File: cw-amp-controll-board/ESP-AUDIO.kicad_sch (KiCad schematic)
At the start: 0 parts

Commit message: finisched ESP32 Audio, started placement
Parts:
- added C10, C11, C16, C9: 100nF, Capacitor_SMD:C_0805_2012Metric_Pad1.18x1.45mm_HandSolder, symbol Device:C
- added C12, C13, C14, C15, C17, C18: 1µF, Capacitor_SMD:C_0805_2012Metric_Pad1.18x1.45mm_HandSolder, symbol Device:C
- added C8: 10µF, Capacitor_SMD:C_0805_2012Metric_Pad1.18x1.45mm_HandSolder, symbol Device:C
- added J4: Conn_01x03_Male, Connector_PinHeader_2.54mm:PinHeader_1x03_P2.54mm_Vertical, symbol Connector:Conn_01x03_Male
- added R19: 470R, Resistor_SMD:R_0805_2012Metric_Pad1.20x1.40mm_HandSolder, symbol Device:R
- added R20: ~, Resistor_SMD:R_0805_2012Metric_Pad1.20x1.40mm_HandSolder, symbol Device:R
- added STAR2: SolderJumper_2_Bridged, Jumper:SolderJumper-2_P1.3mm_Bridged_RoundedPad1.0x1.5mm, symbol Jumper:SolderJumper_2_Bridged
- added U6: PCM5100A, Package_SO:TSSOP-20_4.4x6.5mm_P0.65mm, symbol Audio:PCM5100
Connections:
- new net: C13.1, C15.1, U6.2 (CAPP)
- new net: C13.2, C15.2, U6.4 (CAPM)
- new net +3V3: C10.1, C11.1, C8.1, C9.1, U6.1 (CPVDD), U6.17 (XSMT), U6.20 (DVDD), U6.8 (AVDD)
- new net BCK: U6.13 (BCK)
- new net DIN: U6.14 (DIN)
- new net GNDA: C11.2, C17.2, C18.2, J4.2 (Pin_2), STAR2.2 (B), U6.9 (AGND)
- new net GNDD: C10.2, C12.2, C14.2, C16.2, C8.2, C9.2, STAR2.1 (A), U6.10 (DEMP), U6.11 (FLT), U6.16 (FMT), U6.19 (DGND), U6.3 (CPGND)
- new net L-OUT-ESP: C17.1, J4.1 (Pin_1), R19.2
- new net LDOO: C16.1, U6.18 (LDOO)
- new net LRCLK: U6.15 (LRCK)
- new net OUTL-PCM: R19.1, U6.6 (OUTL)
- new net OUTR-PCM: R20.1, U6.7 (OUTR)
- new net R-OUT-ESP: C18.1, J4.3 (Pin_3), R20.2
- new net SCK: U6.12 (SCK)
- new net VNEG: C12.1, C14.1, U6.5 (VNEG)

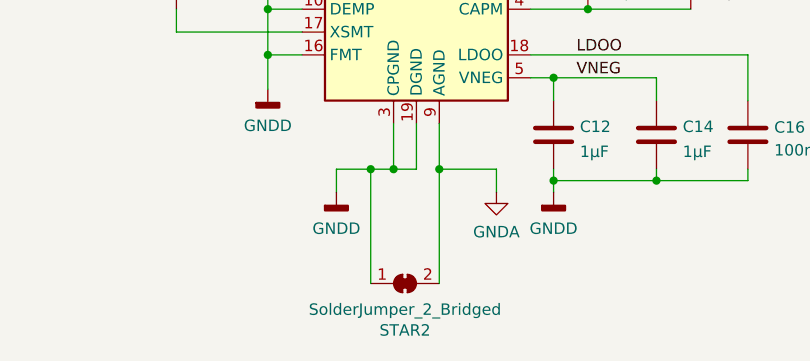
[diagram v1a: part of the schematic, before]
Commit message: reqork for 1.2, fix error with i2c port expander
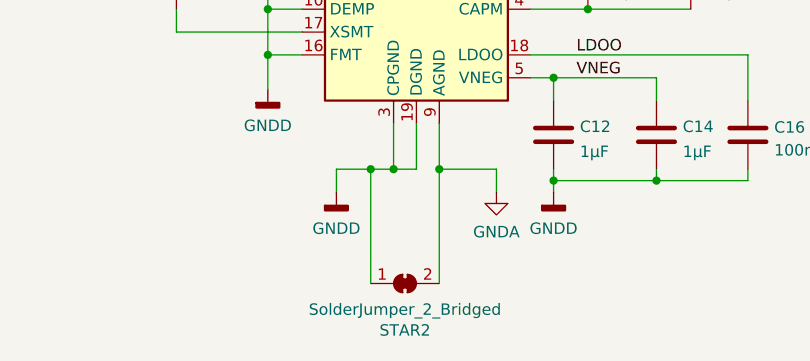
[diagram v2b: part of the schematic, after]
